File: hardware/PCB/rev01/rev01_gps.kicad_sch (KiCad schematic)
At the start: 14 parts, among them J5 GPS_ANT, U1 NEO-M8N

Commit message: pcb progress
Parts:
- C1, C7: footprint Capacitor_SMD:C_0603_1608Metric -> Capacitor_SMD:C_0805_2012Metric
- C2: footprint Capacitor_SMD:C_0402_1005Metric -> Capacitor_SMD:C_0603_1608Metric
- C26: footprint Capacitor_SMD:C_0805_2012Metric -> Capacitor_SMD:C_0402_1005Metric
- D4: footprint LED_SMD:LED_1206_3216Metric -> LED_SMD:LED_0603_1608Metric
- L3: footprint CI160808_33NJ:INDC1608X08N -> Inductor_SMD:L_0603_1608Metric
- R17, R23, R24: footprint Resistor_SMD:R_0402_1005Metric -> Resistor_SMD:R_0603_1608Metric
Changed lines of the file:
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@@
 			)
 		)
-		(property "Footprint" "Capacitor_SMD:C_0805_2012Metric"
+		(property "Footprint" "Capacitor_SMD:C_0402_1005Metric"
 			(at 179.324 121.793 0)
 			(effects
@@
 			)
 		)
-		(property "Footprint" "Resistor_SMD:R_0402_1005Metric"
+		(property "Footprint" "Resistor_SMD:R_0603_1608Metric"
 			(at 227.457 69.977 90)
 			(effects
@@
 			)
 		)
-		(property "Footprint" "Capacitor_SMD:C_0603_1608Metric"
+		(property "Footprint" "Capacitor_SMD:C_0805_2012Metric"
 			(at 114.3 149.479 0)
 			(effects
@@
 			)
 		)
-		(property "Footprint" "Capacitor_SMD:C_0603_1608Metric"
+		(property "Footprint" "Capacitor_SMD:C_0805_2012Metric"
 			(at 82.042 56.007 0)
 			(effects
@@
 			)
 		)
-		(property "Footprint" "LED_SMD:LED_1206_3216Metric"
+		(property "Footprint" "LED_SMD:LED_0603_1608Metric"
 			(at 229.235 80.899 0)
 			(effects
@@
 			)
 		)
-		(property "Footprint" "CI160808_33NJ:INDC1608X08N"
+		(property "Footprint" "Inductor_SMD:L_0603_1608Metric"
 			(at 179.324 114.427 0)
 			(effects
@@
 			)
 		)
-		(property "Footprint" "Resistor_SMD:R_0402_1005Metric"
+		(property "Footprint" "Resistor_SMD:R_0603_1608Metric"
 			(at 186.944 114.935 90)
 			(effects
@@
 			)
 		)
-		(property "Footprint" "Resistor_SMD:R_0402_1005Metric"
+		(property "Footprint" "Resistor_SMD:R_0603_1608Metric"
 			(at 215.646 67.183 0)
 			(effects
@@
 			)
 		)
-		(property "Footprint" "Capacitor_SMD:C_0402_1005Metric"
+		(property "Footprint" "Capacitor_SMD:C_0603_1608Metric"
 			(at 128.143 149.479 0)
 			(effects

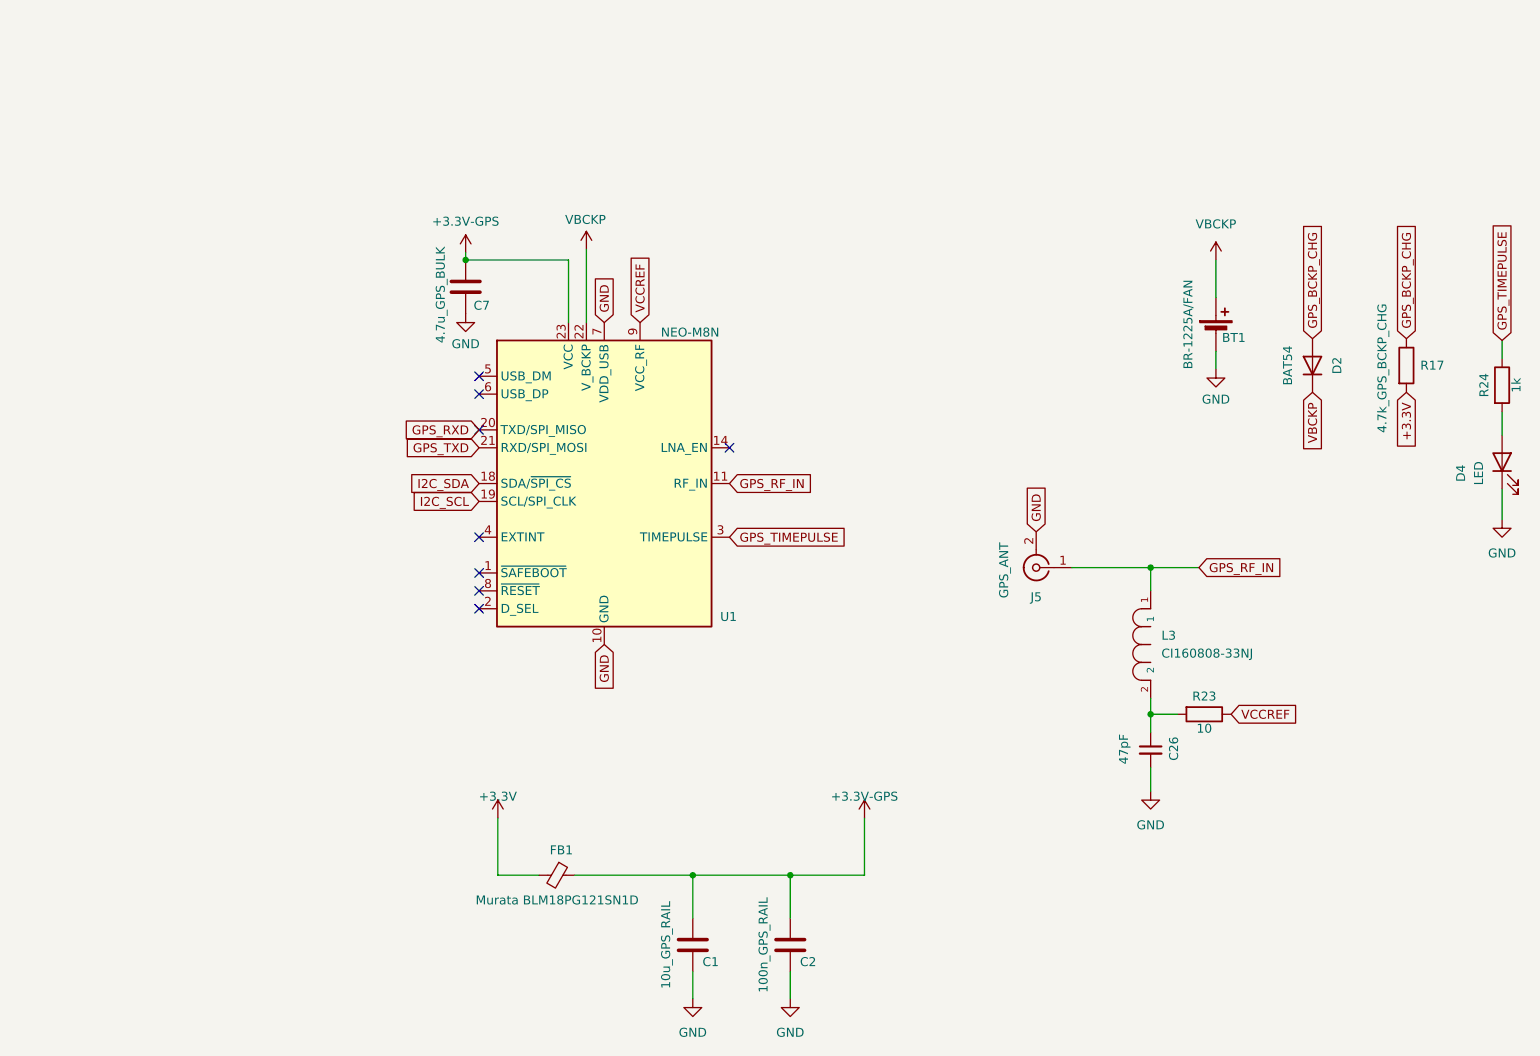
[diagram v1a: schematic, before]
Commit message: added e-paper display
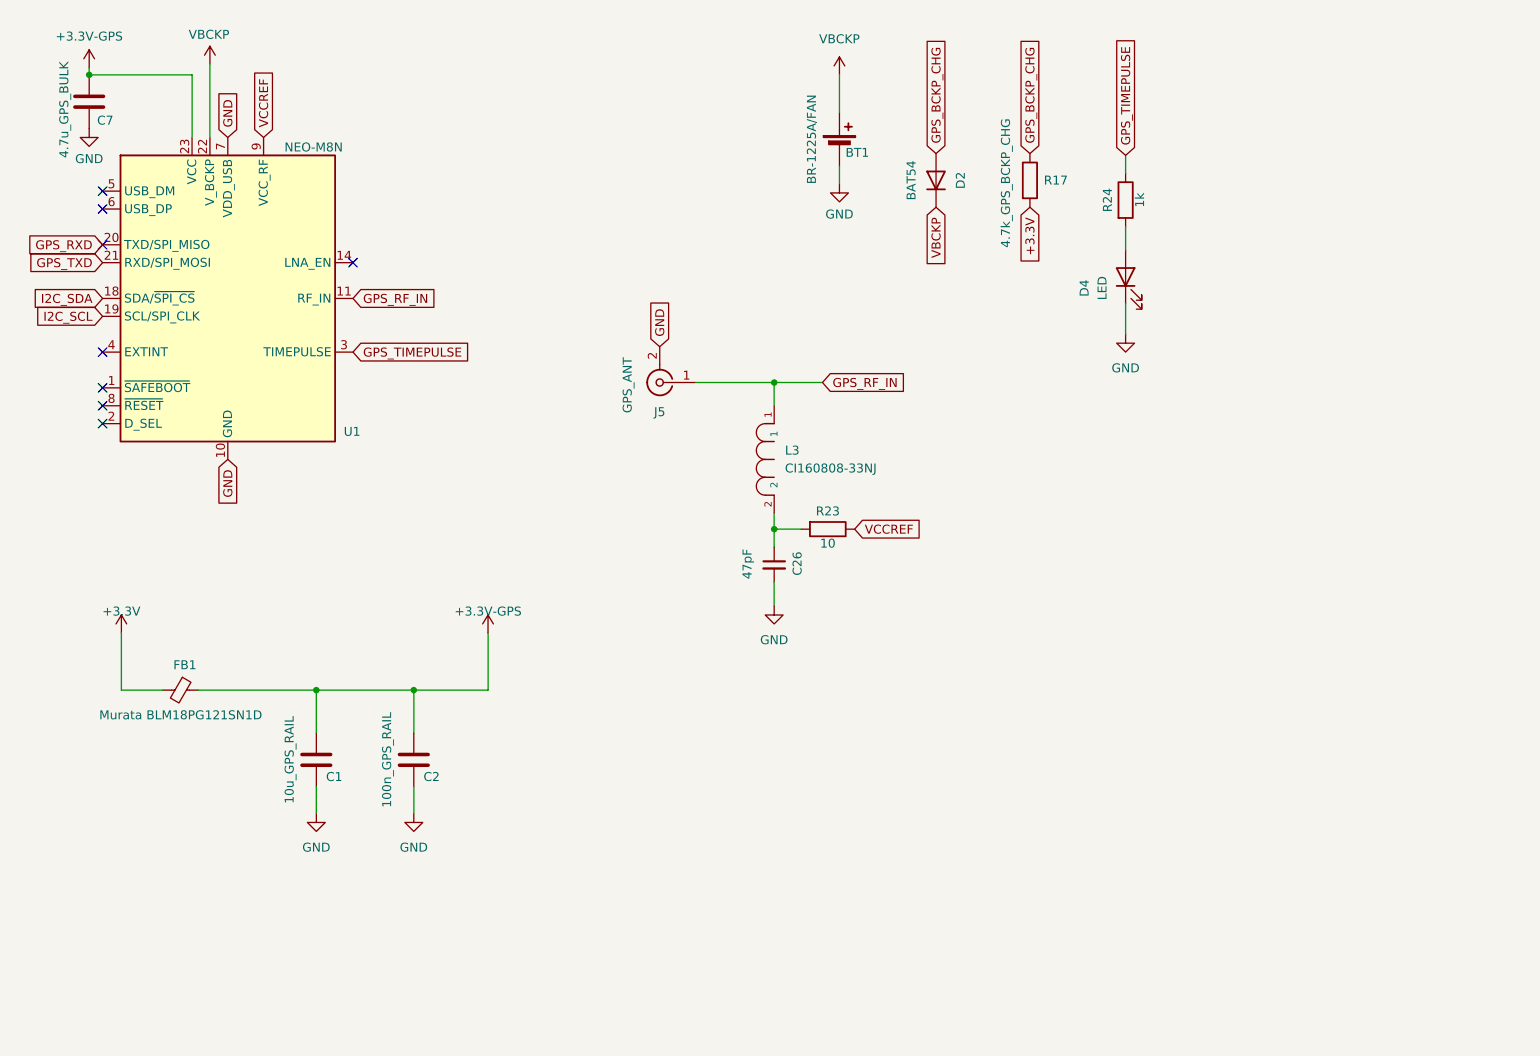
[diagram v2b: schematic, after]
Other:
- moved on the sheet: BT1, C1, C2, C26, C7, D2, D4, FB1, J5, L3, R17, R23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
